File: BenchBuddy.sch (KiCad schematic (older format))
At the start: 0 parts

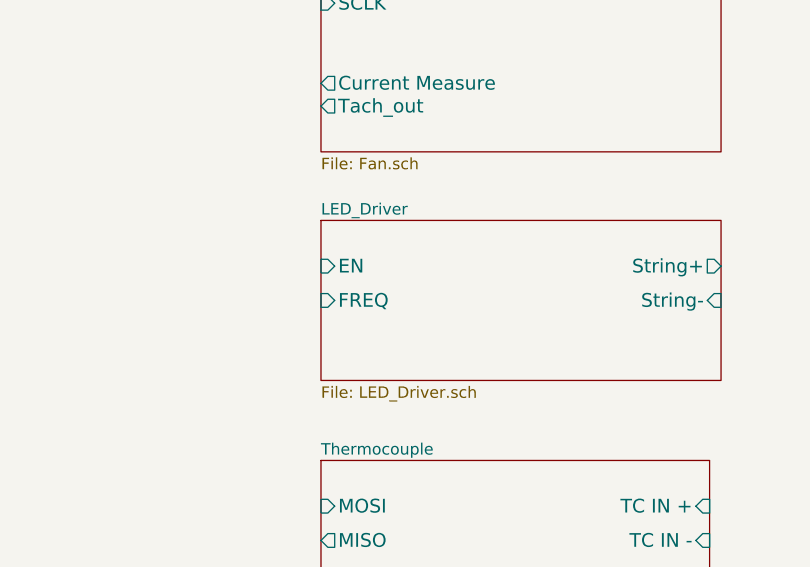
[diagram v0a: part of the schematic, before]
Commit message: Added LED Circuit
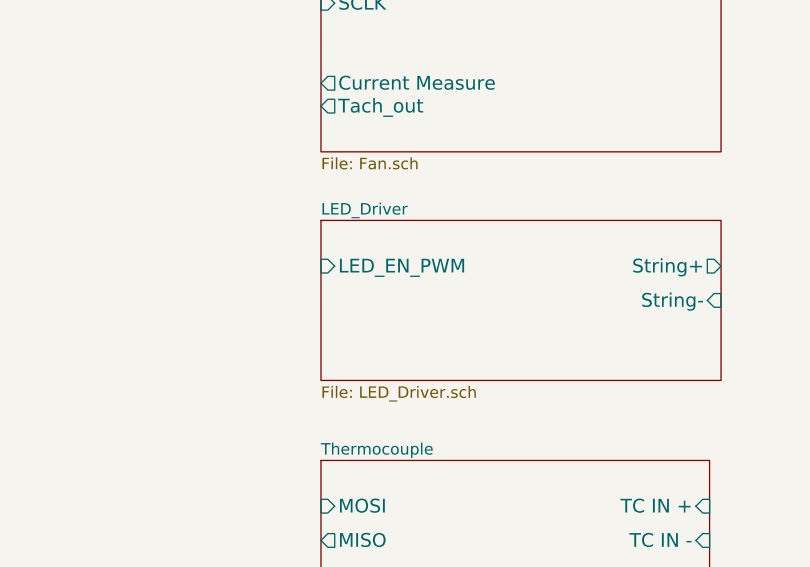
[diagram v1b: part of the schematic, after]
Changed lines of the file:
@@
-EESchema Schematic File Version 2  date 9/21/2013 6:30:50 PM
+EESchema Schematic File Version 2  date 9/22/2013 4:01:30 PM
 LIBS:power
 LIBS:device
@@
 Sheet 1 9
 Title "noname.sch"
-Date "21 sep 2013"
+Date "22 sep 2013"
 Rev ""
 Comp ""
@@
 F0 "LED_Driver" 50
 F1 "LED_Driver.sch" 50
-F2 "EN" I L 7750 3800 60
-F3 "FREQ" I L 7750 3950 60
-F4 "String+" O R 9500 3800 60
-F5 "String-" I R 9500 3950 60
+F2 "String+" O R 9500 3800 60
+F3 "String-" I R 9500 3950 60
+F4 "LED_EN_PWM" I L 7750 3800 60
 $EndSheet
 $Sheet

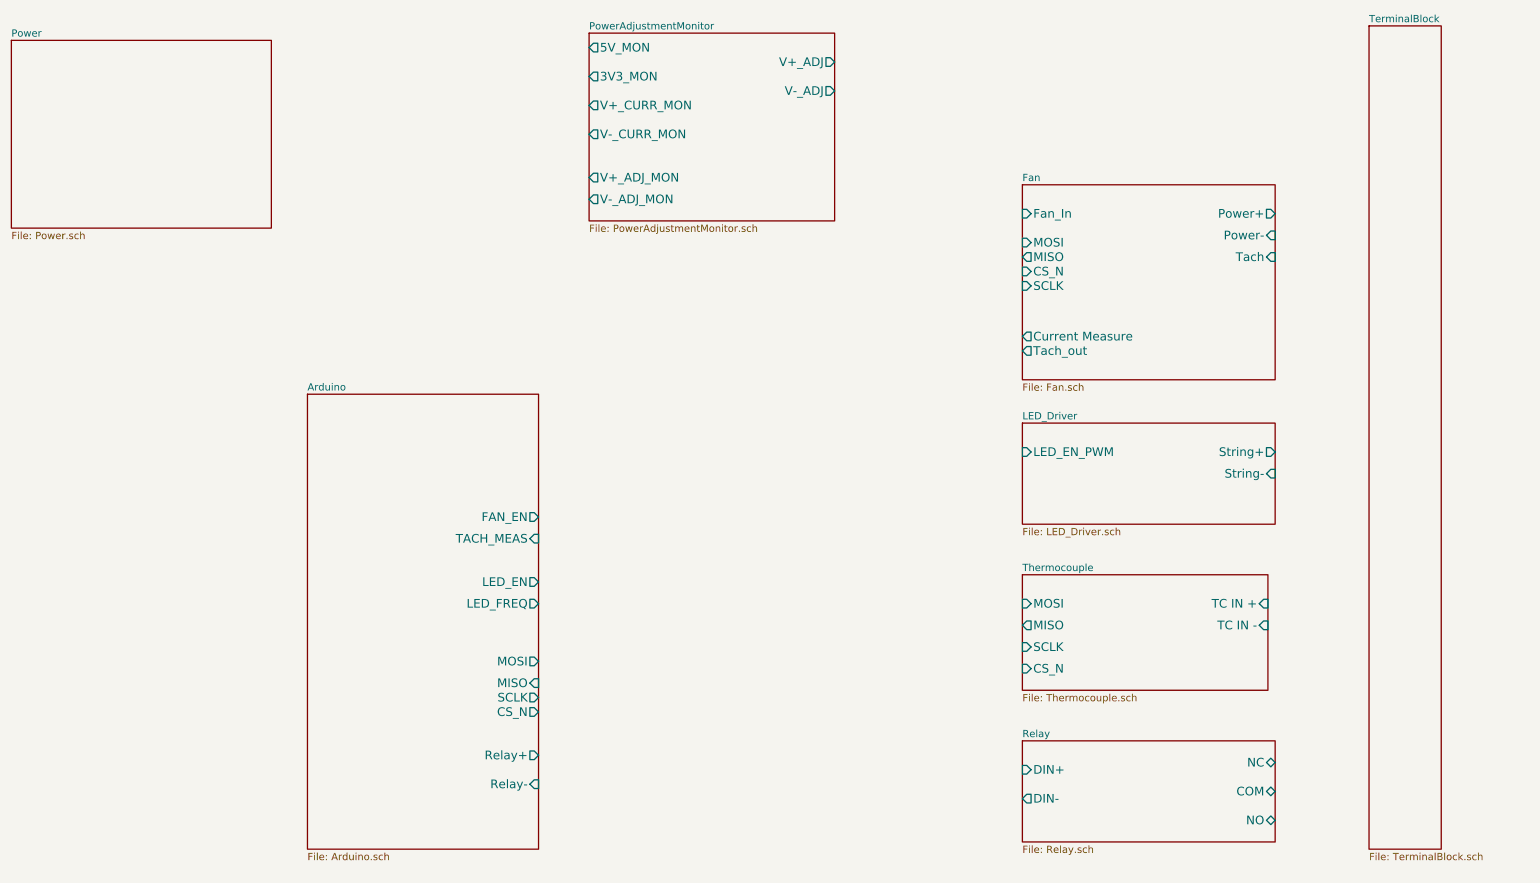
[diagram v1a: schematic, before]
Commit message: Added Arduino Module and Connected Top Level
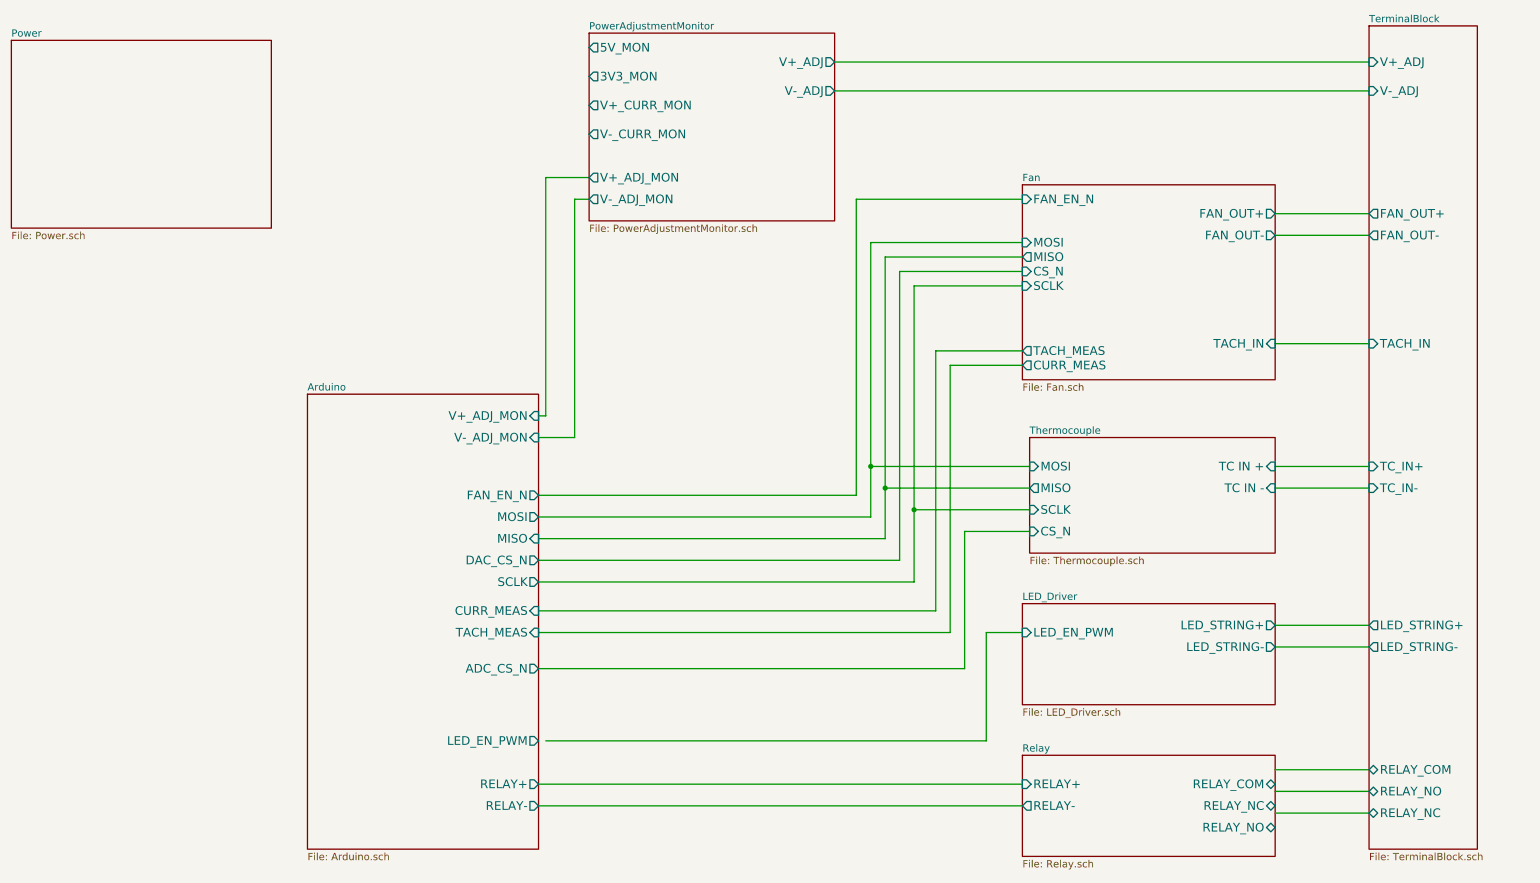
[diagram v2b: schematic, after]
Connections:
- wire segments 0 -> 50
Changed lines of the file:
@@
-EESchema Schematic File Version 2  date 9/22/2013 4:01:30 PM
+EESchema Schematic File Version 2  date 9/22/2013 9:40:39 PM
 LIBS:power
 LIBS:device
@@
 Sheet 1 9
 Title "noname.sch"
-Date "22 sep 2013"
+Date "23 sep 2013"
 Rev ""
 Comp ""
@@
 $EndDescr
 $Sheet
-S 2800 3400 1600 3150
-U 522FEA6C
-F0 "Arduino" 50
-F1 "Arduino.sch" 50
-F2 "Relay+" O R 4400 5900 60
-F3 "Relay-" I R 4400 6100 60
-F4 "MOSI" O R 4400 5250 60
-F5 "MISO" I R 4400 5400 60
-F6 "SCLK" O R 4400 5500 60
-F7 "CS_N" O R 4400 5600 60
-F8 "LED_EN" O R 4400 4700 60
-F9 "LED_FREQ" O R 4400 4850 60
-F10 "FAN_EN" O R 4400 4250 60
-F11 "TACH_MEAS" I R 4400 4400 60
-$EndSheet
-$Sheet
-S 7750 4650 1700 800
+S 7800 3700 1700 800
 U 522FEABA
 F0 "Thermocouple" 50
 F1 "Thermocouple.sch" 50
-F2 "TC IN +" I R 9450 4850 60
-F3 "TC IN -" I R 9450 5000 60
-F4 "MOSI" I L 7750 4850 60
-F5 "MISO" O L 7750 5000 60
-F6 "SCLK" I L 7750 5150 60
-F7 "CS_N" I L 7750 5300 60
+F2 "TC IN +" I R 9500 3900 60
+F3 "TC IN -" I R 9500 4050 60
+F4 "MOSI" I L 7800 3900 60
+F5 "MISO" O L 7800 4050 60
+F6 "SCLK" I L 7800 4200 60
+F7 "CS_N" I L 7800 4350 60
 $EndSheet
 $Sheet
@@
 F0 "Fan" 50
 F1 "Fan.sch" 50
-F2 "Power+" O R 9500 2150 60
-F3 "Power-" I R 9500 2300 60
-F4 "Tach" I R 9500 2450 60
-F5 "Tach_out" O L 7750 3100 60
-F6 "Fan_In" I L 7750 2150 60
-F7 "Current Measure" O L 7750 3000 60
-F8 "MOSI" I L 7750 2350 60
-F9 "MISO" O L 7750 2450 60
-F10 "CS_N" I L 7750 2550 60
-F11 "SCLK" I L 7750 2650 60
-$EndSheet
-$Sheet
-S 7750 3600 1750 700
+F2 "MOSI" I L 7750 2350 60
+F3 "MISO" O L 7750 2450 60
+F4 "CS_N" I L 7750 2550 60
+F5 "SCLK" I L 7750 2650 60
+F6 "FAN_OUT+" O R 9500 2150 60
+F7 "TACH_IN" I R 9500 3050 60
+F8 "TACH_MEAS" O L 7750 3100 60
+F9 "FAN_EN_N" I L 7750 2050 60
+F10 "CURR_MEAS" O L 7750 3200 60
+F11 "FAN_OUT-" O R 9500 2300 60
+$EndSheet
+$Sheet
+S 7750 4850 1750 700
 U 522FEB12
 F0 "LED_Driver" 50
 F1 "LED_Driver.sch" 50
-F2 "String+" O R 9500 3800 60
-F3 "String-" I R 9500 3950 60
-F4 "LED_EN_PWM" I L 7750 3800 60
-$EndSheet
-$Sheet
-S 7750 5800 1750 700
+F2 "LED_EN_PWM" I L 7750 5050 60
+F3 "LED_STRING+" O R 9500 5000 60
+F4 "LED_STRING-" O R 9500 5150 60
+$EndSheet
+$Sheet
+S 7750 5900 1750 700
 U 522FEAC6
 F0 "Relay" 50
 F1 "Relay.sch" 50
-F2 "DIN+" I L 7750 6000 60
-F3 "DIN-" O L 7750 6200 60
-F4 "NC" B R 9500 5950 60
-F5 "NO" B R 9500 6350 60
-F6 "COM" B R 9500 6150 60
-$EndSheet
-$Sheet
-S 10150 850  500  5700
-U 522FEB54
-F0 "TerminalBlock" 50
-F1 "TerminalBlock.sch" 50
+F2 "RELAY_NC" B R 9500 6250 60
+F3 "RELAY_NO" B R 9500 6400 60
+F4 "RELAY_COM" B R 9500 6100 60
+F5 "RELAY+" I L 7750 6100 60
+F6 "RELAY-" O L 7750 6250 60
 $EndSheet
 $Sheet
@@
 F9 "V+_CURR_MON" O L 4750 1400 60
 $EndSheet
+$Sheet
+S 10150 850  750  5700
+U 522FEB54
+F0 "TerminalBlock" 50
+F1 "TerminalBlock.sch" 50
+F2 "V+_ADJ" I L 10150 1100 60
+F3 "V-_ADJ" I L 10150 1300 60
+F4 "FAN_OUT+" O L 10150 2150 60
+F5 "FAN_OUT-" O L 10150 2300 60
+F6 "TACH_IN" I L 10150 3050 60
+F7 "LED_STRING+" O L 10150 5000 60
+F8 "LED_STRING-" O L 10150 5150 60
+F9 "TC_IN+" I L 10150 3900 60
+F10 "TC_IN-" I L 10150 4050 60
+F11 "RELAY_COM" B L 10150 6000 60
+F12 "RELAY_NO" B L 10150 6150 60
+F13 "RELAY_NC" B L 10150 6300 60
+$EndSheet
+$Sheet
+S 2800 3400 1600 3150
+U 522FEA6C
+F0 "Arduino" 50
+F1 "Arduino.sch" 50
+F2 "MOSI" O R 4400 4250 60
+F3 "MISO" I R 4400 4400 60
+F4 "SCLK" O R 4400 4700 60
+F5 "TACH_MEAS" I R 4400 5050 60
+F6 "RELAY+" O R 4400 6100 60
+F7 "RELAY-" O R 4400 6250 60
+F8 "FAN_EN_N" O R 4400 4100 60
+F9 "CURR_MEAS" I R 4400 4900 60
+F10 "V+_ADJ_MON" I R 4400 3550 60
+F11 "V-_ADJ_MON" I R 4400 3700 60
+F12 "LED_EN_PWM" O R 4400 5800 60
+F13 "DAC_CS_N" O R 4400 4550 60
+F14 "ADC_CS_N" O R 4400 5300 60
+$EndSheet
+Wire Wire Line
+	10150 1100 6450 1100
+Wire Wire Line
+	6450 1300 10150 1300
+Wire Wire Line
+	9500 2150 10150 2150
+Wire Wire Line
+	10150 2300 9500 2300
+Wire Wire Line
+	9500 3050 10150 3050
+Wire Wire Line
+	9500 6000 10150 6000
+Wire Wire Line
+	10150 6150 9500 6150
+Wire Wire Line
+	9500 6300 10150 6300
+Wire Wire Line
+	4400 3550 4450 3550
+Wire Wire Line
+	4450 3550 4450 1900
+Wire Wire Line
+	4450 1900 4750 1900
+Wire Wire Line
+	4400 3700 4650 3700
+Wire Wire Line
+	4650 3700 4650 2050
+Wire Wire Line
+	4650 2050 4750 2050
+Wire Wire Line
+	4400 4100 6600 4100
+Wire Wire Line
+	6600 4100 6600 2050
+Wire Wire Line
+	6600 2050 7750 2050
+Wire Wire Line
+	7750 2350 6700 2350
+Wire Wire Line
+	6700 2350 6700 4250
+Wire Wire Line
+	6700 4250 4400 4250
+Wire Wire Line
+	7750 2450 6800 2450
+Wire Wire Line
+	6800 2450 6800 4400
+Wire Wire Line
+	6800 4400 4400 4400
+Wire Wire Line
+	7750 2550 6900 2550
+Wire Wire Line
+	6900 2550 6900 4550
+Wire Wire Line
+	7000 2650 7000 4700
+Wire Wire Line
+	7000 4700 4400 4700
+Wire Wire Line
+	7750 3100 7150 3100
+Wire Wire Line
+	7150 3100 7150 4900
+Wire Wire Line
+	7150 4900 4400 4900
+Wire Wire Line
+	7750 3200 7250 3200
+Wire Wire Line
+	7250 3200 7250 5050
+Wire Wire Line
+	7250 5050 4400 5050
+Wire Wire Line
+	7800 3900 6700 3900
+Connection ~ 6700 3900
+Wire Wire Line
+	7800 4050 6800 4050
+Connection ~ 6800 4050
+Wire Wire Line
+	6900 4550 4400 4550
+Wire Wire Line
+	7800 4350 7350 4350
+Wire Wire Line
+	7350 4350 7350 5300
+Wire Wire Line
+	7350 5300 4400 5300
+Wire Wire Line
+	4450 5800 7500 5800
+Wire Wire Line
+	7500 5800 7500 5050
+Wire Wire Line
+	7500 5050 7750 5050
+Wire Wire Line
+	7750 6100 4400 6100
+Wire Wire Line
+	4400 6250 7750 6250
+Wire Wire Line
+	10150 3900 9500 3900
+Wire Wire Line
+	10150 4050 9500 4050
+Wire Wire Line
+	10150 5150 9500 5150
+Wire Wire Line
+	9500 5000 10150 5000
+Wire Wire Line
+	7750 2650 7000 2650
+Wire Wire Line
+	7800 4200 7000 4200
+Connection ~ 7000 4200
 $EndSCHEMATC
